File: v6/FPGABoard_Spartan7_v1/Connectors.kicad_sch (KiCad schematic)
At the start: 1 part

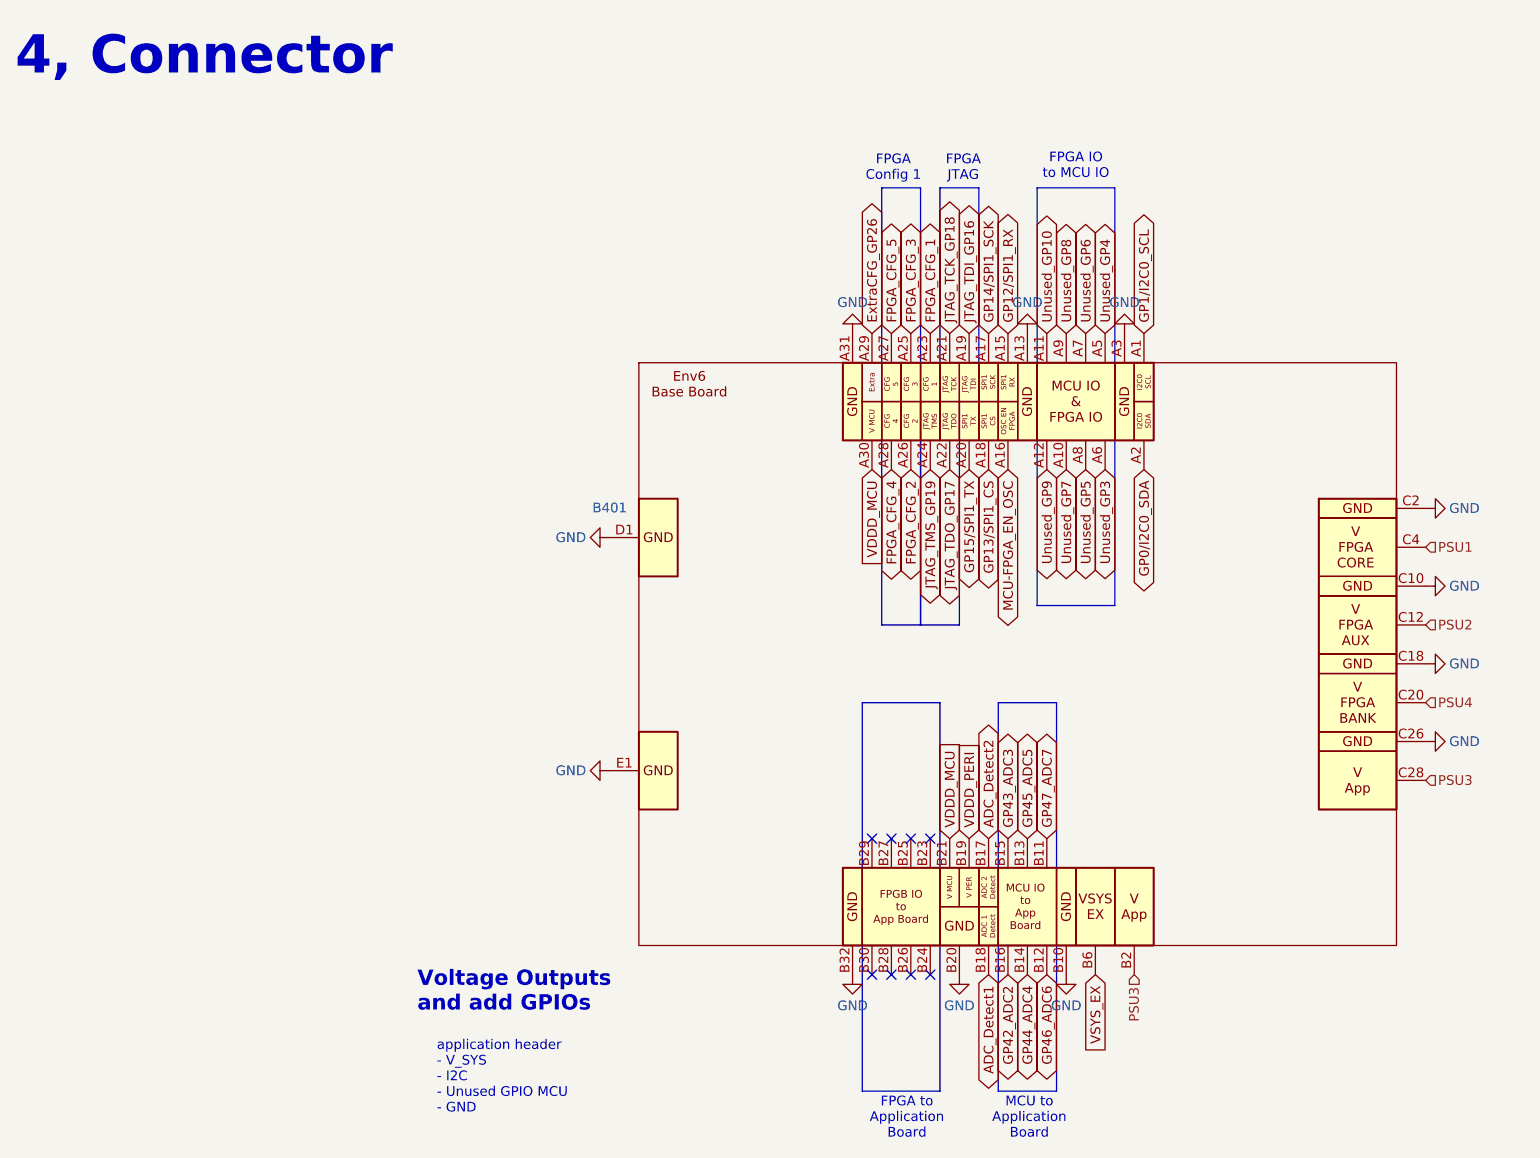
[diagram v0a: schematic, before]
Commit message: SPartan7Board and new Symbol and Footprint
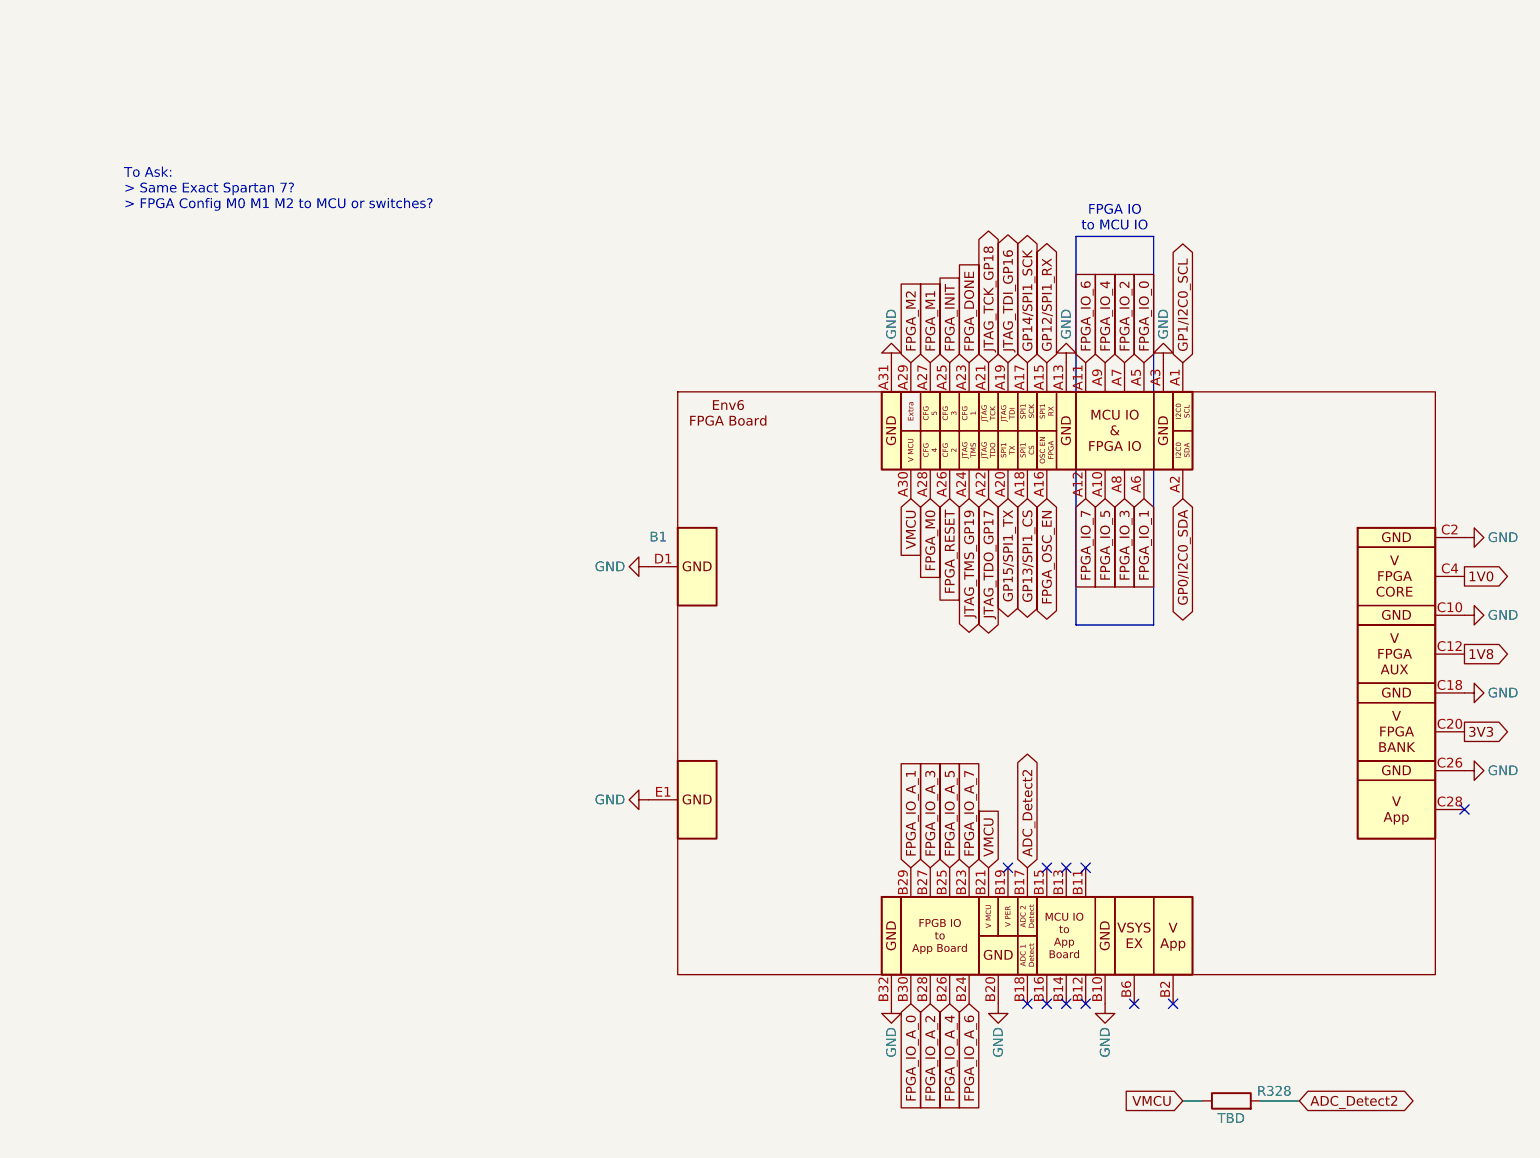
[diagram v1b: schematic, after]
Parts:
- removed B401: (no value), ENv6_Custom_Footprints:BaseBoard_ENv6, symbol ENv6_Custom_Symbols:BaseBoard_ENv6
- added B1: (no value), ENv6_Custom_Footprints:ExtensionBoard_ENv6, symbol ENv6_Custom_Symbols:FPGABoard_ENv6
- added R328: TBD, Resistor_SMD:R_0402_1005Metric, symbol passive:R0402
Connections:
- net ADC_Detect2: now also B1.B17, R328.2
- net GND: now also B1.A13, B1.A14, B1.A3, B1.A31, B1.A32, B1.A4, B1.B10, B1.B20, B1.B22, B1.B31, B1.B32, B1.B9, B1.C1, B1.C10, B1.C17, B1.C18, B1.C2, B1.C25, B1.C26, B1.C9, B1.D1, B1.D2, B1.D3, B1.D4, B1.D5, B1.D6, B1.D7, B1.D8, B1.E1, B1.E2, B1.E3, B1.E4, B1.E5, B1.E6, B1.E7, B1.E8
- net GP0/I2C0_SDA: now also B1.A2
- net GP12/SPI1_RX: now also B1.A15
- net GP13/SPI1_CS: now also B1.A18
- net GP14/SPI1_SCK: now also B1.A17
- net GP15/SPI1_TX: now also B1.A20
- net GP1/I2C0_SCL: now also B1.A1
- net JTAG_TCK_GP18: now also B1.A21
- net JTAG_TDI_GP16: now also B1.A19
- net JTAG_TDO_GP17: now also B1.A22
- net JTAG_TMS_GP19: now also B1.A24
- new net: B1.B1, B1.B2, B1.B3, B1.B4
- new net: B1.B5, B1.B6, B1.B7, B1.B8
- new net: B1.C27, B1.C28, B1.C29, B1.C30, B1.C31, B1.C32
- new net 1V0: B1.C3, B1.C4, B1.C5, B1.C6, B1.C7, B1.C8
- new net 1V8: B1.C11, B1.C12, B1.C13, B1.C14, B1.C15, B1.C16
- new net 3V3: B1.C19, B1.C20, B1.C21, B1.C22, B1.C23, B1.C24
- new net FPGA_DONE: B1.A23
- new net FPGA_INIT: B1.A25
- new net FPGA_IO_0: B1.A5
- new net FPGA_IO_1: B1.A6
- new net FPGA_IO_2: B1.A7
- new net FPGA_IO_3: B1.A8
- new net FPGA_IO_4: B1.A9
- new net FPGA_IO_5: B1.A10
- new net FPGA_IO_6: B1.A11
- new net FPGA_IO_7: B1.A12
- new net FPGA_IO_A_0: B1.B30
- new net FPGA_IO_A_1: B1.B29
- new net FPGA_IO_A_2: B1.B28
- new net FPGA_IO_A_3: B1.B27
- new net FPGA_IO_A_4: B1.B26
- new net FPGA_IO_A_5: B1.B25
- new net FPGA_IO_A_6: B1.B24
- new net FPGA_IO_A_7: B1.B23
- new net FPGA_M0: B1.A28
- new net FPGA_M1: B1.A27
- new net FPGA_M2: B1.A29
- new net FPGA_OSC_EN: B1.A16
- new net FPGA_RESET: B1.A26
- new net VMCU: B1.A30, B1.B21, R328.1
- no-connect marks 8 -> 11
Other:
- note added: "To Ask: > Same Exact Spartan 7? > FPGA Config M0 M1 M2 to MCU or switches?"
- note removed: "4, Connector"
- note removed: "FPGA Config 1"
- note removed: "FPGA JTAG"
- note removed: "FPGA to Application Board"
- note removed: "MCU to Application Board"
- note removed: "Voltage Outputs and add GPIOs"
- note removed: "application header - V_SYS - I2C - Unused GPIO MCU - GND"
